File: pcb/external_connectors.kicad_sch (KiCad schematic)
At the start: 2 parts, among them J11 Conn_01x04_Pin_P2.54mm, J12 Conn_01x04_Qwiic

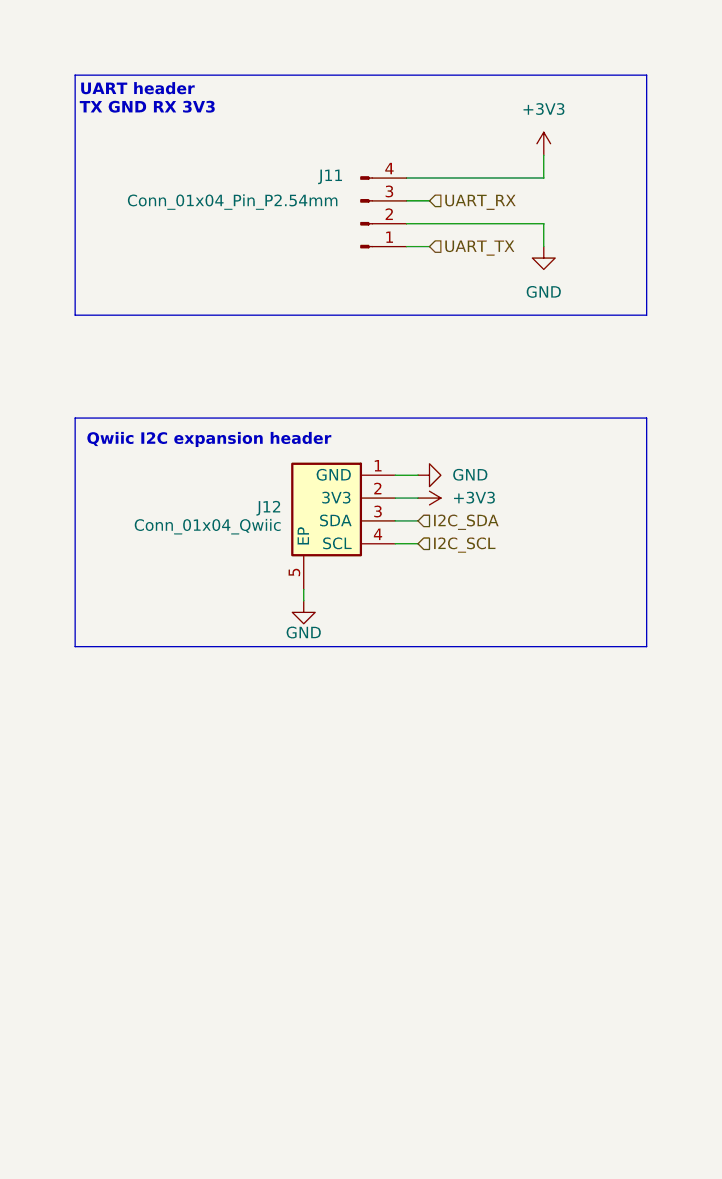
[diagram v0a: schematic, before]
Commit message: Improve inter sheet connections
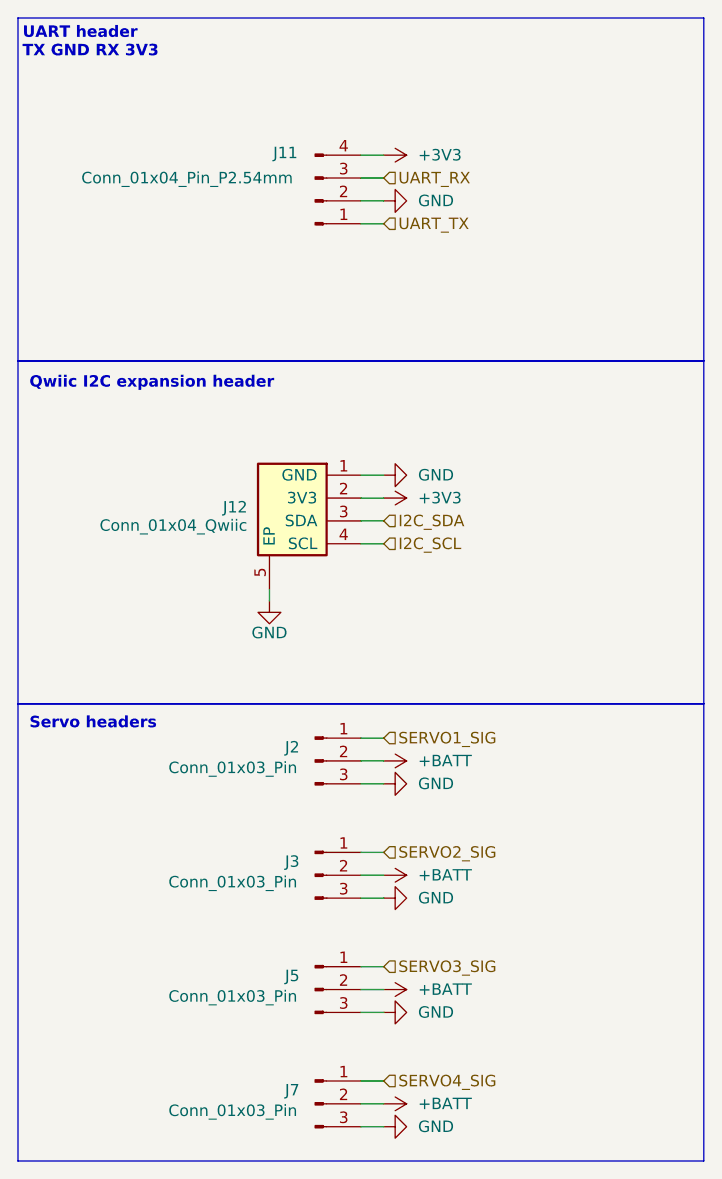
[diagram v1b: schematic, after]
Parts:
- added J2, J3, J5, J7: Conn_01x03_Pin, symbol Connector:Conn_01x03_Pin
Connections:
- net GND: now also J2.3 (Pin_3), J3.3 (Pin_3), J5.3 (Pin_3), J7.3 (Pin_3)
- new net +BATT: J2.2 (Pin_2), J3.2 (Pin_2), J5.2 (Pin_2), J7.2 (Pin_2)
- new net SERVO1_SIG: J2.1 (Pin_1)
- new net SERVO2_SIG: J3.1 (Pin_1)
- new net SERVO3_SIG: J5.1 (Pin_1)
- new net SERVO4_SIG: J7.1 (Pin_1)
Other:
- note added: "Servo headers"
- title: (none) -> Flight Computer
- moved on the sheet: J11, J12

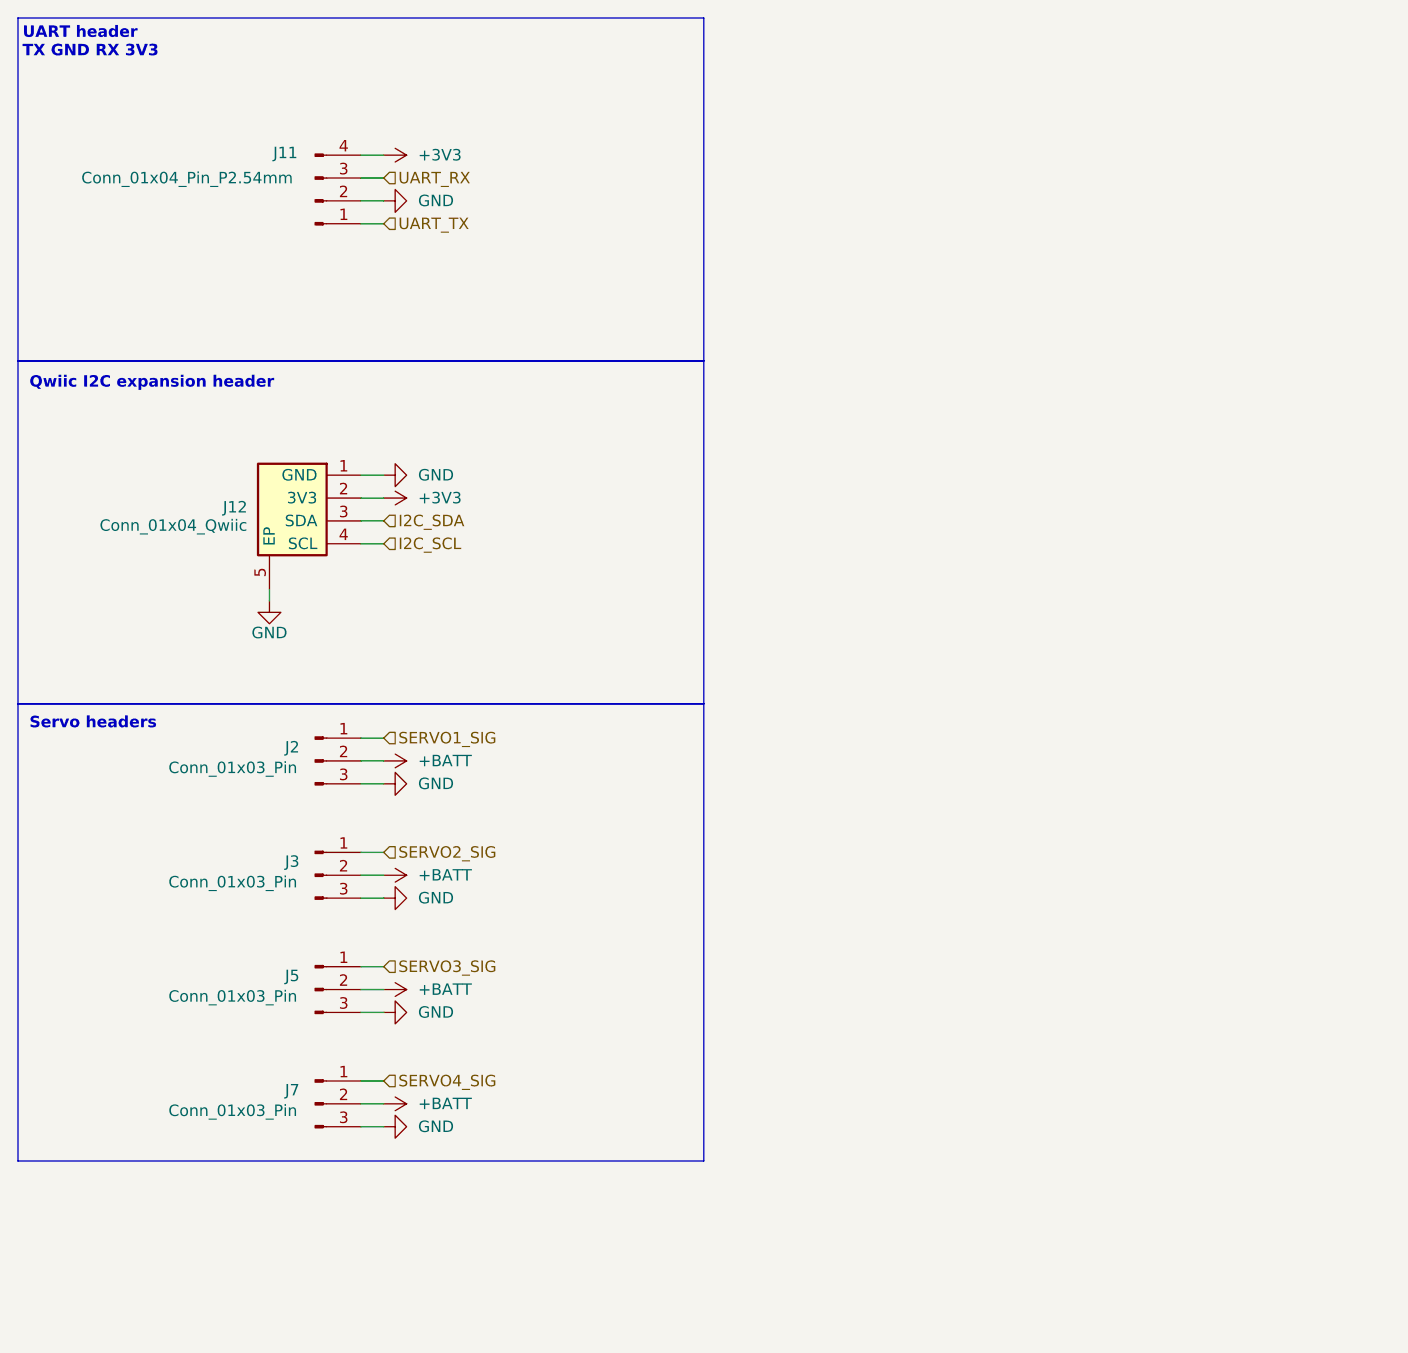
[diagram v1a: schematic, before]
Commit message: Add external pin header
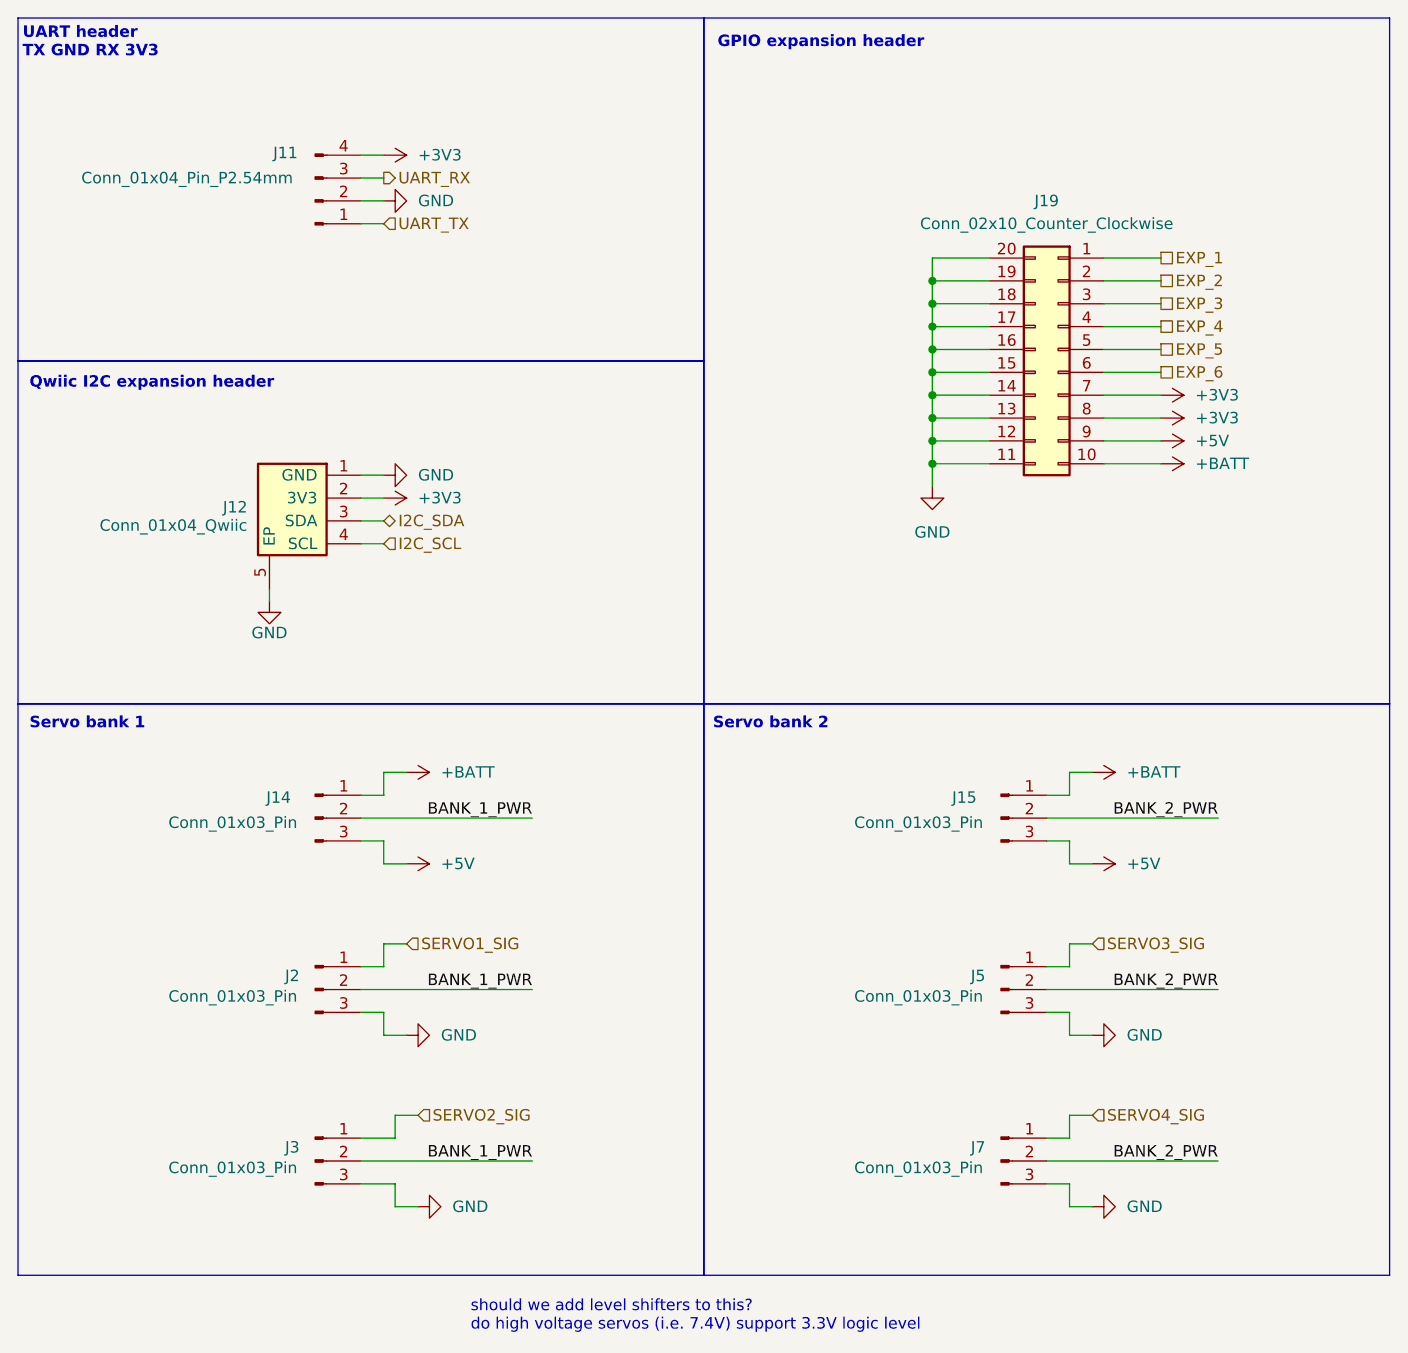
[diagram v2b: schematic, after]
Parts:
- added J14, J15: Conn_01x03_Pin, symbol Connector:Conn_01x03_Pin
- added J19: Conn_02x10_Counter_Clockwise, symbol Connector_Generic:Conn_02x10_Counter_Clockwise
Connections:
- net +3V3: now also J19.7 (Pin_7), J19.8 (Pin_8)
- net +BATT: now also J14.1 (Pin_1), J15.1 (Pin_1), J19.10 (Pin_10); no longer J2.2 (Pin_2), J3.2 (Pin_2), J5.2 (Pin_2), J7.2 (Pin_2)
- net GND: now also J19.11 (Pin_11), J19.12 (Pin_12), J19.13 (Pin_13), J19.14 (Pin_14), J19.15 (Pin_15), J19.16 (Pin_16), J19.17 (Pin_17), J19.18 (Pin_18), J19.19 (Pin_19), J19.20 (Pin_20)
- new net +5V: J14.3 (Pin_3), J15.3 (Pin_3), J19.9 (Pin_9)
- new net BANK_1_PWR: J14.2 (Pin_2), J2.2 (Pin_2), J3.2 (Pin_2)
- new net BANK_2_PWR: J15.2 (Pin_2), J5.2 (Pin_2), J7.2 (Pin_2)
- new net EXP_1: J19.1 (Pin_1)
- new net EXP_2: J19.2 (Pin_2)
- new net EXP_3: J19.3 (Pin_3)
- new net EXP_4: J19.4 (Pin_4)
- new net EXP_5: J19.5 (Pin_5)
- new net EXP_6: J19.6 (Pin_6)
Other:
- note added: "GPIO expansion header"
- note added: "Servo bank 1"
- note added: "Servo bank 2"
- note added: "should we add level shifters to this? do high voltage servos (i.e. 7.4V) support 3.3V logic level"
- note removed: "Servo headers"
- moved on the sheet: J2, J3, J5, J7

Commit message: Assign most footprints
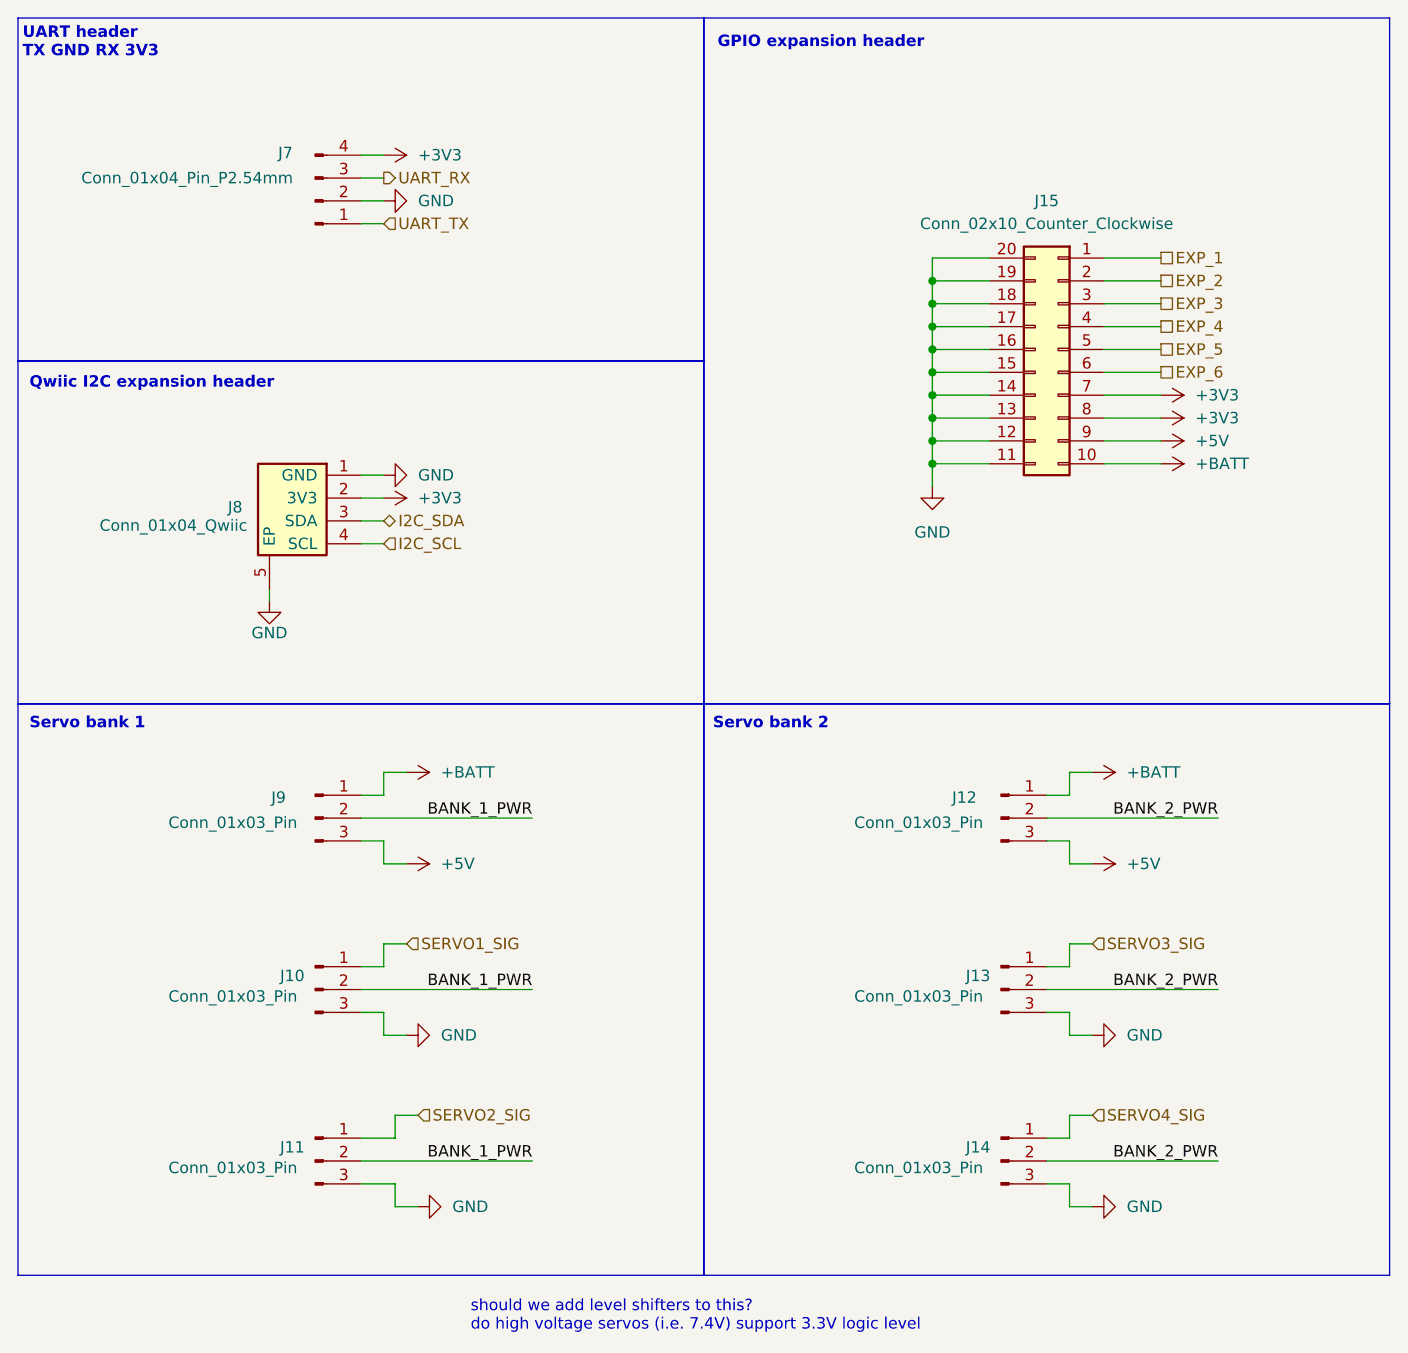
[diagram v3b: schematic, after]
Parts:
- J10: renamed from J2; footprint (none) -> Connector_PinHeader_2.54mm:PinHeader_1x03_P2.54mm_Vertical
- J11: renamed from J3; footprint (none) -> Connector_PinHeader_2.54mm:PinHeader_1x03_P2.54mm_Vertical
- J12: renamed from J15; footprint (none) -> Connector_PinHeader_2.54mm:PinHeader_1x03_P2.54mm_Vertical
- J13: renamed from J5; footprint (none) -> Connector_PinHeader_2.54mm:PinHeader_1x03_P2.54mm_Vertical
- J14: renamed from J7; footprint (none) -> Connector_PinHeader_2.54mm:PinHeader_1x03_P2.54mm_Vertical
- J15: renamed from J19; footprint (none) -> Connector_PinHeader_2.54mm:PinHeader_2x10_P2.54mm_Vertical
- J7: renamed from J11; footprint (none) -> Connector_PinHeader_2.54mm:PinHeader_1x04_P2.54mm_Vertical
- J9: renamed from J14; footprint (none) -> Connector_PinHeader_2.54mm:PinHeader_1x03_P2.54mm_Vertical
- renumbered J12 to J8
